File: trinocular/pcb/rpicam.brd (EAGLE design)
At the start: 65 x 56 mm, 13 parts, among them IC1 MEGA8-AI, X1 C-GRID-03-70553

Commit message: trinocular: PCB rev.3 - wip
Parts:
- removed SV3: (no value), con-lstb:MA04-1
- removed U$1: LED0603, wb:D0603
- removed U$2: (no value), RaspberryPi:RPICAM
- added I2C: (no value), con-maritex:MICROMATCH-4
- added LED1: (no value), led:CHIP-LED0805
- added U$4: (no value), RaspberryPi:RPICAM_WAVESHARE
- C1: device rcl:C0603 -> rcl:C0805
- R1: device rcl:R0603 -> rcl:R0805
- SV1: device con-lstb:MA20-2 -> con-lstb:MA04-1
- moved SV2 72.9 mm to (-1.60, -16.0), turned to 0 degrees
- moved SV1 71.5 mm to (-1.60, -10.4)
- moved X2 66.6 mm to (71.4, 16.4), turned to 270 degrees
- moved IC1 23.7 mm to (19.6, 10.3)
- moved C1 21.5 mm to (28.3, 11.5)
- moved ISP 14.2 mm to (3.90, 15.3)
- moved X1 12.8 mm to (46.4, -4.00), turned to 180 degrees
- moved UART 8.66 mm to (-2.50, 43.6)
- moved R1 2.42 mm to (17.2, 36.3)
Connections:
- new net +18V: SV1.2, SV2.2, X2.1
- net +5V: now also I2C.4, LED1.A, SV2.4; no longer SV1.2, SV2.1, SV2.3, SV3.1, SV3.3, U$1.1, X2.1
- net GND: now also I2C.3, SV1.1, SV2.1; no longer SV1.14, SV1.20, SV1.25, SV1.30, SV1.34, SV1.39, SV1.6, SV1.9, SV2.4, SV3.4
- net LED1_CTRL: now also SV1.3; no longer SV2.2
- net LED2_CTRL: now also SV2.3; no longer SV3.2
- net N$1: now also LED1.C; no longer U$1.2
- net SCL: now also I2C.2; no longer SV1.5
- net SDA: now also I2C.1; no longer SV1.3
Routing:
- net +5V: track 200.3 -> 0.00 mm
- net MOSI/SRV_CTRL: track 64.9 -> 0.00 mm, vias 1 -> 0
- net LED1_CTRL: track 63.4 -> 0.00 mm, vias 1 -> 0
- net LED2_CTRL: track 40.0 -> 0.00 mm, vias 1 -> 0
- net RST: track 29.0 -> 0.00 mm, vias 1 -> 0
- net SDA: track 28.4 -> 0.00 mm
- net SCL: track 26.9 -> 0.00 mm
- net MISO: track 24.6 -> 0.00 mm, vias 1 -> 0
- net RXD: track 21.3 -> 0.00 mm, vias 1 -> 0
- net SCK: track 20.3 -> 0.00 mm
- net TXD: track 20.1 -> 0.00 mm, vias 1 -> 0
- net N$4: track 6.02 -> 0.00 mm
- net N$1: track 1.60 -> 0.00 mm
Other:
- board size 65 x 56 mm -> 65 x 82.8 mm

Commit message: trinocular: PCB v3 - wip
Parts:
- removed I2C: (no value), con-maritex:MICROMATCH-4
- removed UART: uart, con-molex:70553-03
- added SV3: (no value), con-lstb:MA03-2
- added SV4: (no value), con-lstb:MA03-1
- moved SV1 79.2 mm to (61.4, 37.6), flipped to the bottom, turned to 270 degrees
- moved SV2 73.5 mm to (61.4, 21.8), flipped to the bottom, turned to 90 degrees
- moved X2 67.7 mm to (3.80, 12.0), flipped to the bottom, turned to 90 degrees
- moved R1 20.8 mm to (3.30, 20.8), turned to 270 degrees
- moved LED1 20.7 mm to (1.40, 20.8), turned to 180 degrees
- moved C1 19.4 mm to (9.80, 17.3), turned to 0 degrees
- moved ISP 15.6 mm to (3.50, 30.9)
- moved X1 7.50 mm to (51.8, 1.20)
- moved IC1 2.86 mm to (16.8, 10.9)
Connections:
- net +5V: now also SV3.4; no longer I2C.4
- net GND: now also SV3.3, SV4.1; no longer I2C.3, UART.1
- net RXD: now also SV4.2; no longer UART.2
- net SCL: now also SV3.2; no longer I2C.2
- net SDA: now also SV3.1; no longer I2C.1
- net TXD: now also SV4.3; no longer UART.3
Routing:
- net +18V: track 0.00 -> 99.8 mm
- net LED1_CTRL: track 0.00 -> 91.2 mm
- net MOSI/SRV_CTRL: track 0.00 -> 89.4 mm, vias 0 -> 1
- net LED2_CTRL: track 0.00 -> 70.4 mm
- net +5V: track 0.00 -> 47.6 mm
- net SCL: track 0.00 -> 44.8 mm
- net SDA: track 0.00 -> 41.9 mm
- net MISO: track 0.00 -> 32.1 mm
- net GND: track 0.00 -> 28.7 mm, vias 4 -> 7
- net RST: track 0.00 -> 28.5 mm, vias 0 -> 1
- net SCK: track 0.00 -> 24.5 mm
- net N$4: track 0.00 -> 18.5 mm, vias 0 -> 2
- net TXD: track 0.00 -> 11.4 mm
- net RXD: track 0.00 -> 9.79 mm
- net N$1: track 0.00 -> 1.92 mm
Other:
- board size 65 x 82.8 mm -> 65 x 56 mm

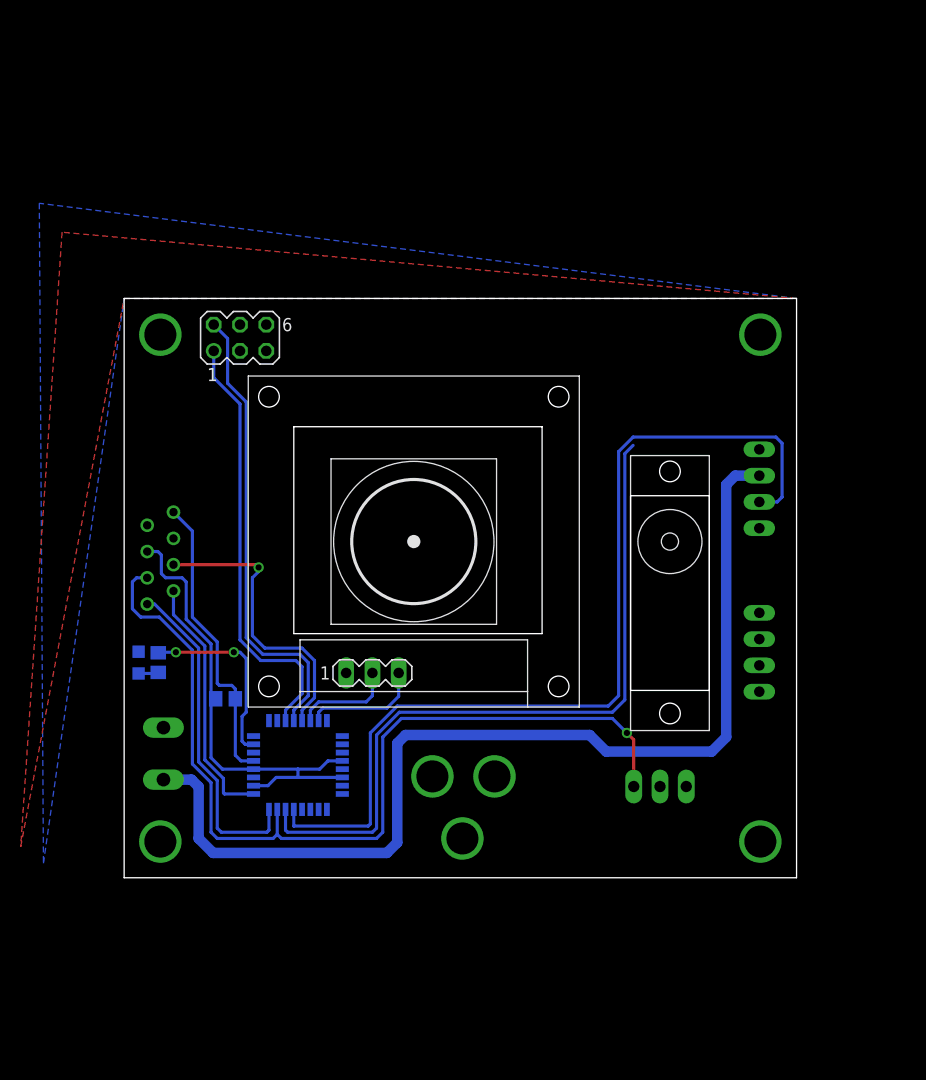
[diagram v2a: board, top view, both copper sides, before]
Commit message: trinocular: rpicam_v3 + gerbers
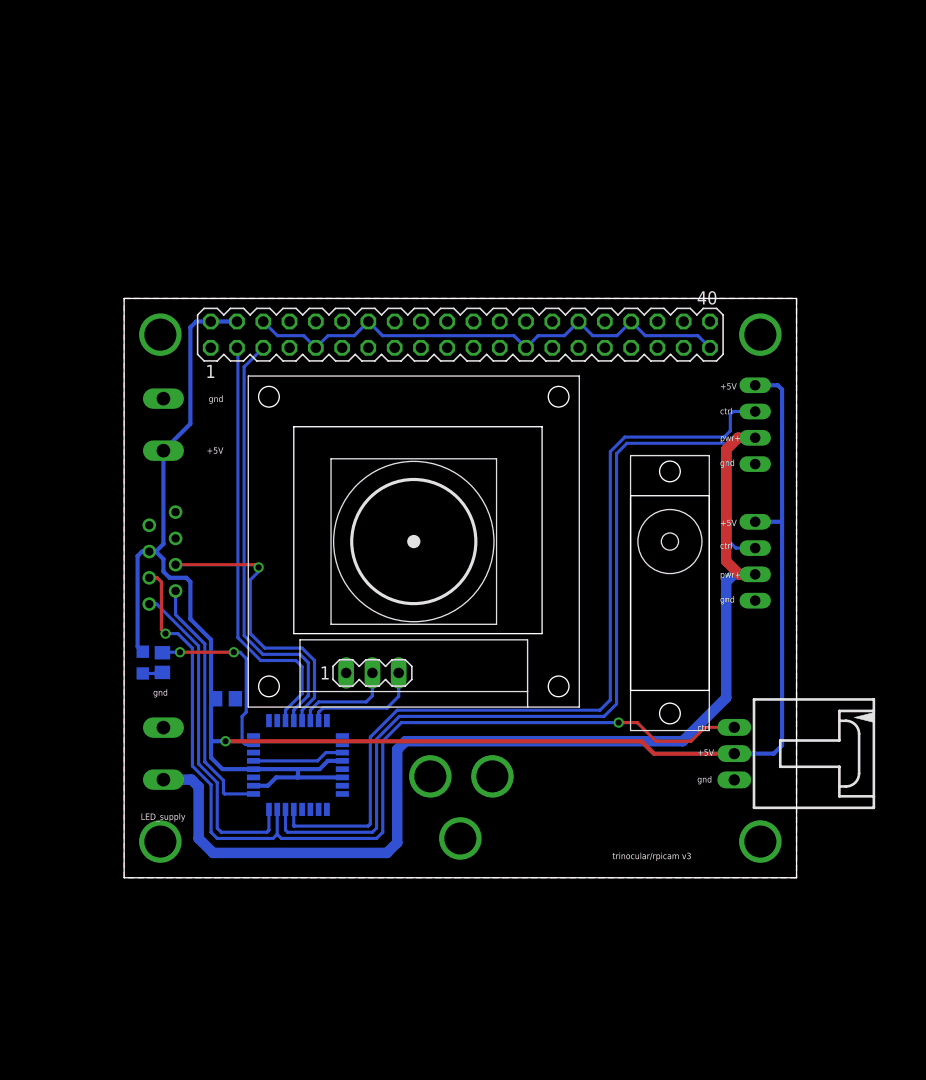
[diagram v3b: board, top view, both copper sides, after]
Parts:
- removed SV3: (no value), con-lstb:MA03-2
- added SV5: (no value), con-lstb:MA20-2
- added X3: (no value), con-ptr500:AK500/2
- moved X1 18.3 mm to (66.6, 12.0), flipped to the top, turned to 270 degrees
- moved SV2 8.81 mm to (61.0, 30.6)
- moved SV1 6.21 mm to (61.0, 43.8), turned to 90 degrees
- moved R1 0.40 mm to (3.70, 20.8)
- moved LED1 0.40 mm to (1.80, 20.8)
- moved ISP 0.20 mm to (3.70, 30.9)
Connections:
- net +5V: now also SV5.2, SV5.4, X3.1; no longer SV3.4
- net GND: now also SV5.14, SV5.25, SV5.30, SV5.34, SV5.39, SV5.6, SV5.9, X3.2; no longer SV3.3
- net SCL: now also SV5.5; no longer SV3.2
- net SDA: now also SV5.3; no longer SV3.1
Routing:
- net +5V: track 47.6 -> 181.6 mm, vias 0 -> 1
- net GND: track 28.7 -> 58.5 mm
- net LED2_CTRL: track 70.4 -> 91.7 mm
- net LED1_CTRL: track 91.2 -> 82.7 mm
- net +18V: track 99.8 -> 103.4 mm
- net MOSI/SRV_CTRL: track 89.4 -> 92.9 mm, vias 1 -> 2
- net SCL: track 44.8 -> 42.1 mm
- net SDA: track 41.9 -> 41.3 mm
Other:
- board text added: "+5V"
- board text added: "LED_supply"
- board text added: "ctrl"
- board text added: "gnd"
- board text added: "pwr+"
- board text added: "rxd"
- board text added: "trinocular/rpicam v3"
- board text added: "txd"
